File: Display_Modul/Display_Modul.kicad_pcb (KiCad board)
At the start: 2 copper layers, 90 x 45 mm, 14 parts, among them J101 Conn_01x08_Male, J102 Conn_02x08_Counter_Clockwise, SW101 Rotary_Encoder_Switch

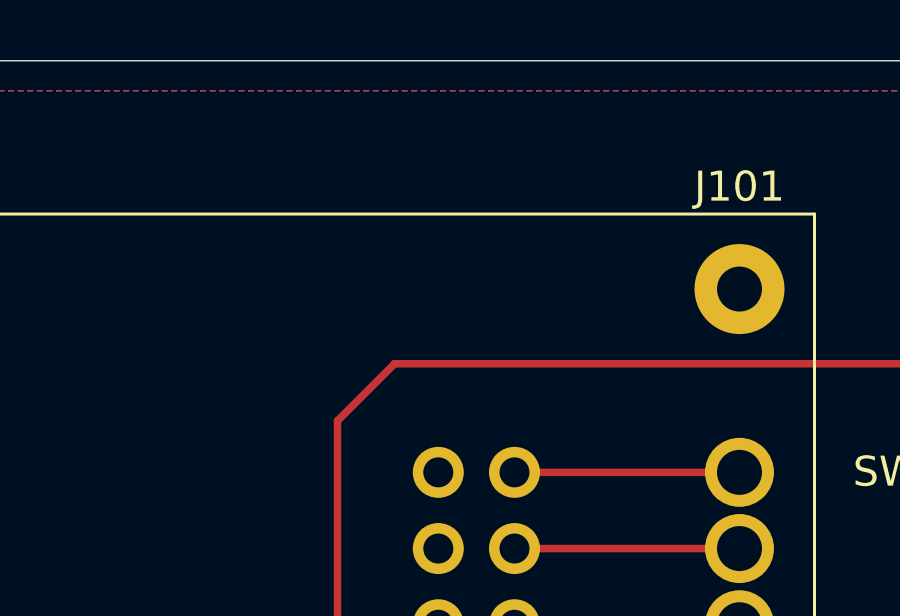
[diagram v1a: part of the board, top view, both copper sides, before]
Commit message: Feeder Rails hinzugefügt
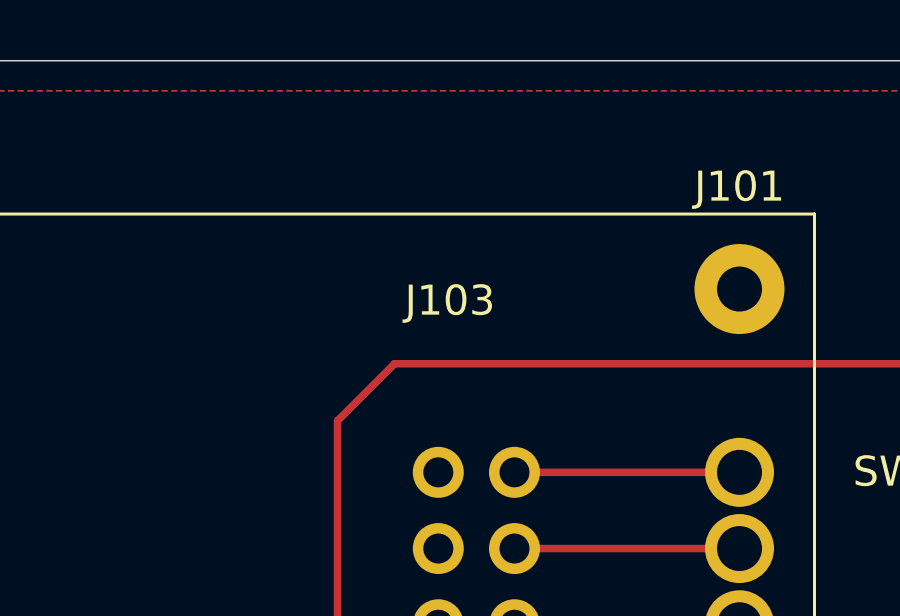
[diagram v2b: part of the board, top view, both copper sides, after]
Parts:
- added J103: IPC 16P, ProjectFootprints:Empty, F.Cu at (151.3, 104.2)
